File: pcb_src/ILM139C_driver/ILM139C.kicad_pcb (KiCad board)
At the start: 4 copper layers, 170 parts, among them CN3 AXE640124D, CN4 AXE640124D, CN5 AXE540127D, CN6 AXE540127D, U1 IS31FL3741A-QFLS4-TR, U10 XL-B1010RGBT-HF, U100 XL-B1010RGBT-HF, U101 XL-B1010RGBT-HF, U102 XL-B1010RGBT-HF, U103 XL-B1010RGBT-HF, U104 XL-B1010RGBT-HF, U105 XL-B1010RGBT-HF, U106 XL-B1010RGBT-HF, U107 XL-B1010RGBT-HF, U108 XL-B1010RGBT-HF, U109 XL-B1010RGBT-HF, U11 XL-B1010RGBT-HF, U110 XL-B1010RGBT-HF, U111 XL-B1010RGBT-HF, U112 XL-B1010RGBT-HF, U113 XL-B1010RGBT-HF, U114 XL-B1010RGBT-HF, U115 XL-B1010RGBT-HF, U116 XL-B1010RGBT-HF, U117 XL-B1010RGBT-HF, U118 XL-B1010RGBT-HF, U12 XL-B1010RGBT-HF, U13 XL-B1010RGBT-HF, U14 XL-B1010RGBT-HF, U15 XL-B1010RGBT-HF, U16 XL-B1010RGBT-HF, U17 XL-B1010RGBT-HF, U18 XL-B1010RGBT-HF, U19 XL-B1010RGBT-HF, U2 XL-B1010RGBT-HF, U20 XL-B1010RGBT-HF, U21 XL-B1010RGBT-HF, U22 XL-B1010RGBT-HF, U23 XL-B1010RGBT-HF, U24 XL-B1010RGBT-HF, U25 XL-B1010RGBT-HF, U26 XL-B1010RGBT-HF, U27 XL-B1010RGBT-HF, U28 XL-B1010RGBT-HF, U29 XL-B1010RGBT-HF, U3 XL-B1010RGBT-HF, U30 XL-B1010RGBT-HF, U31 XL-B1010RGBT-HF, U32 XL-B1010RGBT-HF, U33 XL-B1010RGBT-HF, U34 XL-B1010RGBT-HF, U35 XL-B1010RGBT-HF, U36 XL-B1010RGBT-HF, U37 XL-B1010RGBT-HF, U38 XL-B1010RGBT-HF, U39 XL-B1010RGBT-HF, U4 XL-B1010RGBT-HF, U40 XL-B1010RGBT-HF, U41 XL-B1010RGBT-HF, U42 XL-B1010RGBT-HF, U43 XL-B1010RGBT-HF, U44 XL-B1010RGBT-HF, U45 XL-B1010RGBT-HF, U46 XL-B1010RGBT-HF, U47 XL-B1010RGBT-HF, U48 XL-B1010RGBT-HF, U49 XL-B1010RGBT-HF, U5 XL-B1010RGBT-HF, U50 XL-B1010RGBT-HF, U51 XL-B1010RGBT-HF, U52 XL-B1010RGBT-HF, U53 XL-B1010RGBT-HF, U54 XL-B1010RGBT-HF, U55 XL-B1010RGBT-HF, U56 XL-B1010RGBT-HF, U57 XL-B1010RGBT-HF, U58 XL-B1010RGBT-HF, U59 XL-B1010RGBT-HF, U6 XL-B1010RGBT-HF, U60 XL-B1010RGBT-HF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

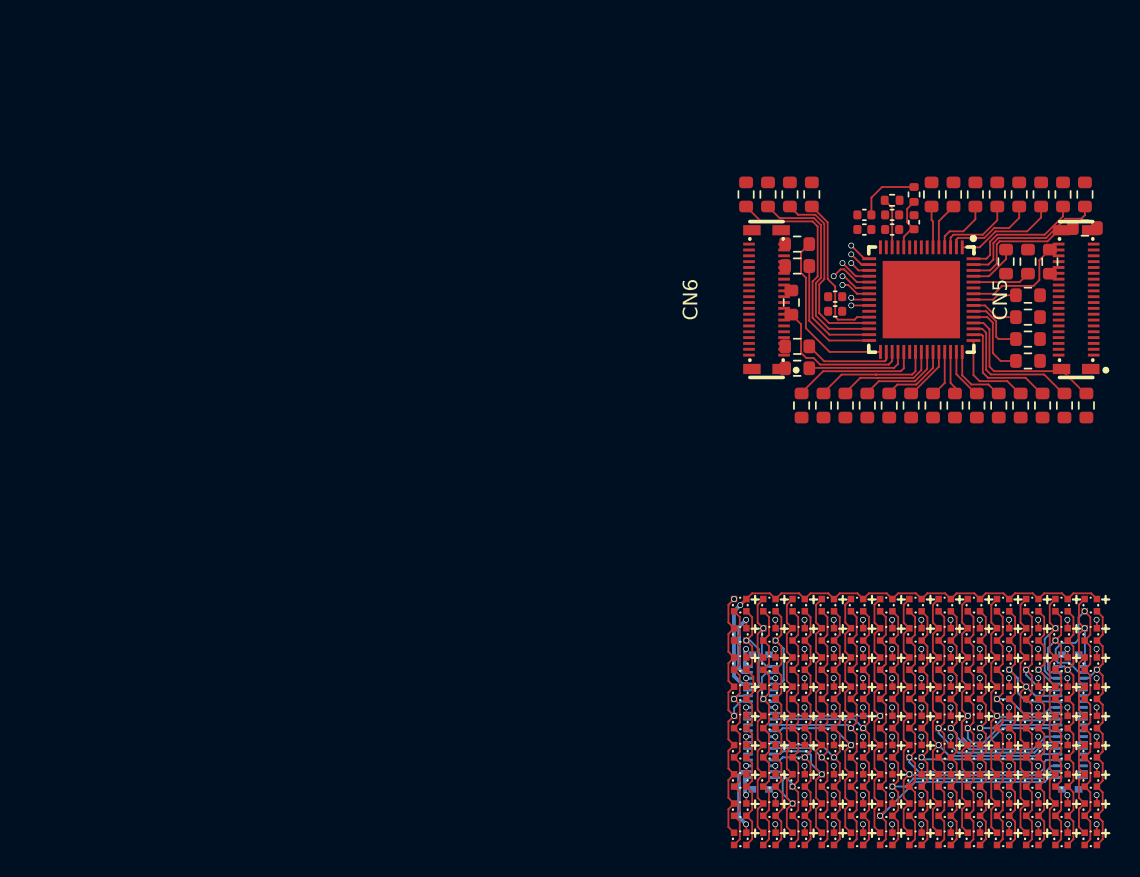
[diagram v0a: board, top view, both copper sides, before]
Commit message: Added driver module
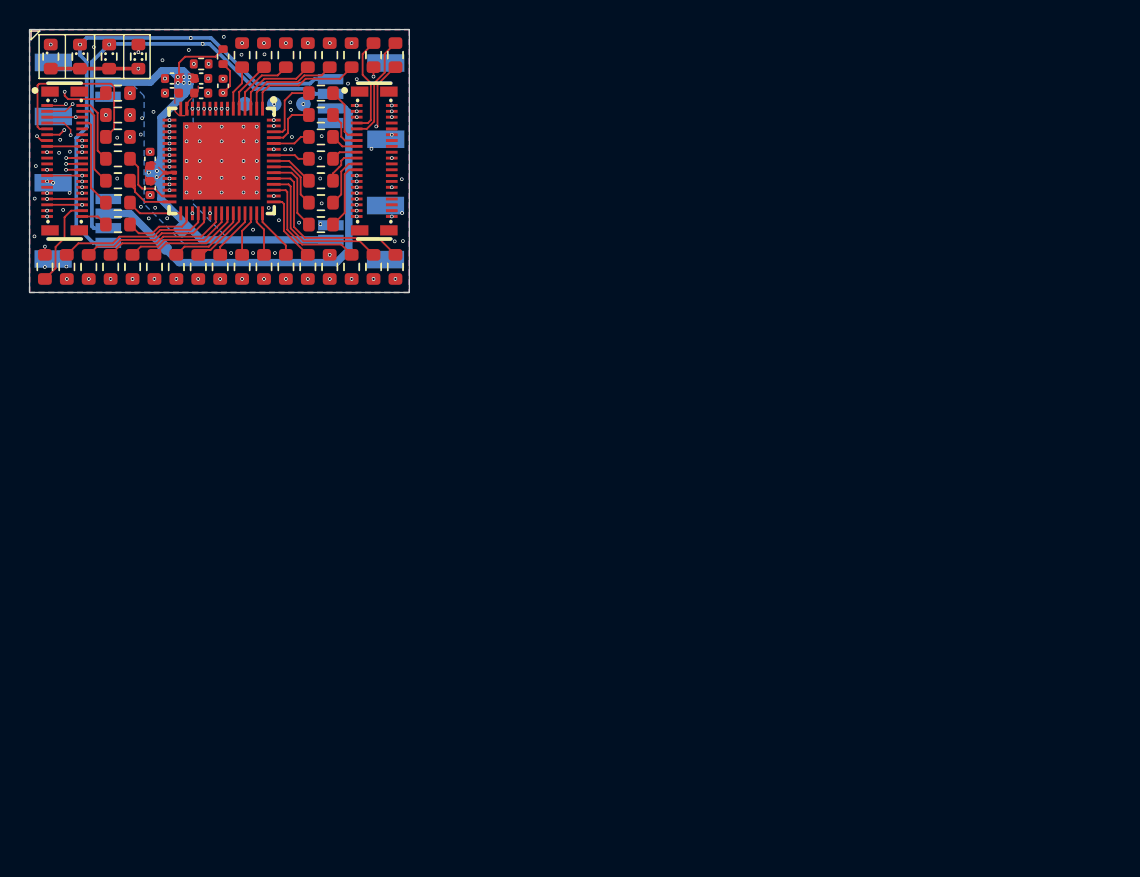
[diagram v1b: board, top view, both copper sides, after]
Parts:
- removed CN3, CN4: AXE640124D, easyeda2kicad:CONN-SMD_40P-P0.40_OK-14GM040-04
- removed U10, U100, U101, U102, U103, U104, U105, U106, U107, U108, U109, U11, U110, U111, U112, U113, U114, U115, U116, U117, U118, U12, U13, U14, U15, U16, U17, U18, U19, U20, U21, U22, U23, U24, U25, U26, U27, U28, U29, U30, U31, U32, U33, U34, U35, U36, U37, U38, U39, U4, U40, U41, U42, U43, U44, U45, U46, U47, U48, U49, U5, U50, U51, U52, U53, U54, U55, U56, U57, U58, U59, U6, U60, U61, U62, U63, U64, U65, U66, U67, U68, U69, U7, U70, U71, U72, U73, U74, U75, U76, U77, U78, U79, U8, U80, U81, U82, U83, U84, U85, U86, U87, U88, U89, U9, U90, U91, U92, U93, U94, U95, U96, U97, U98, U99: XL-B1010RGBT-HF, easyeda2kicad:LED-SMD_4P-L1.0-W1.0-TR_1
- added CN1: HC-1.0-2PWT, easyeda2kicad:CONN-SMD_HC-1.0-2PWT, B.Cu at (93.5, 56.0)
- added CN2: HC-1.0-2PWT, easyeda2kicad:CONN-SMD_HC-1.0-2PWT, B.Cu at (112.5, 65.8)
- added R42: 0, Resistor_SMD:R_0603_1608Metric, F.Cu at (91.4, 53.7)
- added R43: 0, Resistor_SMD:R_0603_1608Metric, F.Cu at (93.4, 53.7)
- added R44: 0, Resistor_SMD:R_0603_1608Metric, F.Cu at (95.4, 53.7)
- added R45: 0, Resistor_SMD:R_0603_1608Metric, F.Cu at (97.4, 53.7)
- added R46: 0, Resistor_SMD:R_0603_1608Metric, B.Cu at (99.8, 66.2)
- added TP1: TestPoint, TestPoint:TestPoint_Pad_D1.0mm, B.Cu at (106.7, 57.0)
- added TP2: TestPoint, TestPoint:TestPoint_Pad_D1.0mm, B.Cu at (104.7, 57.0)
- added TP3: TestPoint, TestPoint:TestPoint_Pad_D1.0mm, B.Cu at (108.7, 57.0)
- U2, U3: value XL-B1010RGBT-HF -> HC-1.0-4PWT-B-HW; footprint easyeda2kicad:LED-SMD_4P-L1.0-W1.0-TR_1 -> easyeda2kicad:CONN-SMD_4P-P1.00_HCTL_HC-1.0-4PWT; moved to B.Cu
- moved U3 53.3 mm to (93.5, 65.0), turned to 90 degrees
- moved R33 53.1 mm to (109.9, 56.2)
- moved R8 51.2 mm to (91.0, 68.1), turned to -90 degrees
- moved R7 50.5 mm to (92.5, 68.1), turned to -90 degrees
- moved R36 50.4 mm to (109.9, 60.7), turned to 0 degrees
- moved R10 49.7 mm to (106.0, 68.1)
- moved R11 49.7 mm to (104.5, 68.1)
- moved R12 49.7 mm to (103.0, 68.1)
- moved R13 49.7 mm to (101.5, 68.1)
- moved R14 49.7 mm to (100.0, 68.1)
- moved R15 49.7 mm to (98.5, 68.1)
- moved R16 49.7 mm to (97.0, 68.1)
- moved R17 49.7 mm to (95.5, 68.1)
- moved R18 49.7 mm to (94.0, 68.1)
- moved R23 49.7 mm to (113.5, 68.1)
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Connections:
- CN5 pad 10: unconnected-(CN5-Pad10) -> GND
- CN5 pad 12: unconnected-(CN5-Pad12) -> GND
- CN5 pad 14: unconnected-(CN5-Pad14) -> GND
- CN5 pad 16: unconnected-(CN5-Pad16) -> GND
- CN5 pad 18: unconnected-(CN5-Pad18) -> GND
- CN5 pad 20: unconnected-(CN5-Pad20) -> GND
- CN5 pad 22: unconnected-(CN5-Pad22) -> GND
- CN5 pad 24: unconnected-(CN5-Pad24) -> GND
- CN5 pad 26: unconnected-(CN5-Pad26) -> GND
- CN5 pad 28: unconnected-(CN5-Pad28) -> GND
- CN5 pad 30: unconnected-(CN5-Pad30) -> GND
- CN5 pad 32: unconnected-(CN5-Pad32) -> GND
- CN5 pad 34: unconnected-(CN5-Pad34) -> GND
- CN5 pad 36: unconnected-(CN5-Pad36) -> GND
- CN5 pad 38: unconnected-(CN5-Pad38) -> GND
- CN5 pad 40: unconnected-(CN5-Pad40) -> GND
- CN5 pad 8: unconnected-(CN5-Pad8) -> GND
- CN6 pad 10: unconnected-(CN6-Pad10) -> GND
- CN6 pad 12: unconnected-(CN6-Pad12) -> GND
- CN6 pad 14: unconnected-(CN6-Pad14) -> GND
- CN6 pad 17: unconnected-(CN6-Pad17) -> GND
- CN6 pad 19: unconnected-(CN6-Pad19) -> GND
- CN6 pad 21: unconnected-(CN6-Pad21) -> GND
- CN6 pad 23: unconnected-(CN6-Pad23) -> GND
- CN6 pad 27: unconnected-(CN6-Pad27) -> GND
- CN6 pad 29: unconnected-(CN6-Pad29) -> GND
- CN6 pad 31: unconnected-(CN6-Pad31) -> GND
- U1 pad 8: GND -> Net-(U1-ADDR)
- U2 pad 1: SW1 -> SCL
- U2 pad 2: S3 -> SDA
- U2 pad 3: S2 -> 3V3
- U2 pad 4: S1 -> GND
- U3 pad 1: SW2 -> SCL
- U3 pad 2: S3 -> SDA
- U3 pad 3: S2 -> 3V3
- U3 pad 4: S1 -> GND
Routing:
- net SCL: track 0.00 -> 53.2 mm, vias 0 -> 3
- net SDA: track 0.00 -> 47.1 mm, vias 0 -> 3
- net VCC: track 4.40 -> 47.1 mm, vias 0 -> 10
- net 3V3: track 0.00 -> 29.0 mm
- net SW2: track 37.4 -> 9.83 mm, vias 14 -> 2
- net SW5: track 34.6 -> 8.72 mm, vias 14 -> 2
- net SW4: track 33.9 -> 8.96 mm, vias 14 -> 2
- net SW9: track 37.5 -> 12.7 mm, vias 14 -> 2
- net SW3: track 34.7 -> 9.99 mm, vias 14 -> 2
- net SW6: track 33.8 -> 9.67 mm, vias 14 -> 2
- net SW1: track 36.3 -> 13.3 mm
- net SW8: track 34.4 -> 11.4 mm, vias 14 -> 2
- net S25: track 27.6 -> 4.73 mm, vias 1 -> 0
- net SW7: track 33.7 -> 11.2 mm, vias 14 -> 2
- net S26: track 26.0 -> 3.64 mm, vias 1 -> 0
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- added copper zone on B.Cu, net GND
- added copper zone on F.Cu, net GND
- added copper zone on In1.Cu, net GND
- added copper zone on In2.Cu, net GND
- added copper zone on B.Cu, net VCC
- added copper zone on F.Cu, net VCC
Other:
- board outline added: 26 x 18 mm
- board text added: "EDrTech"
- board text added: "GND"
- board text added: "ILM139C"
- board text added: "INT"
- board text added: "SDB"
- board text added: "V0.1.0"
- board text added: "⠁ 0x00 ⠉ 0x00 ⠋ 0x00 ⠛ 0x00"

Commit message: QWIIC things added
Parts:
- added G***: LOGO, easyeda2kicad:qwiic_3mm, B.Cu at (113.0, 52.6)
